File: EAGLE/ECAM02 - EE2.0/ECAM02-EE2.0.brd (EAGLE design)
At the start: 82.6 x 75.9 mm, 61 parts, among them J1 MODULAR TOOL, J2 SPI, J3 MOT, J4 FTDI, J5 S4B-PH-SM4, J6 SOL+PUMP, J7 RINGLIGHT, Q2 16MHz, U1 SP3485, U10 MCP4725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

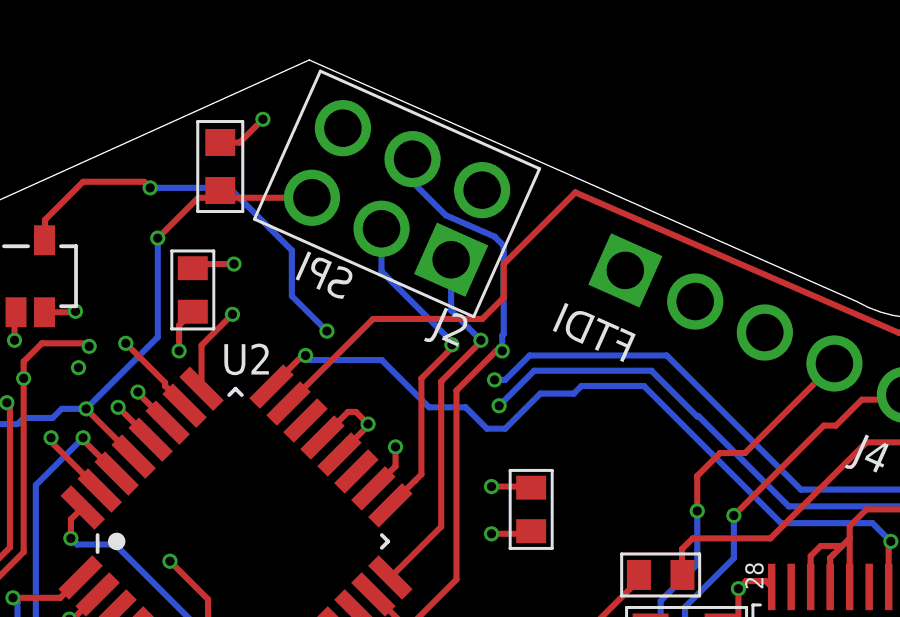
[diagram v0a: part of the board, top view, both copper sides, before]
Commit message: Fixed BOM, began adding DFM changes
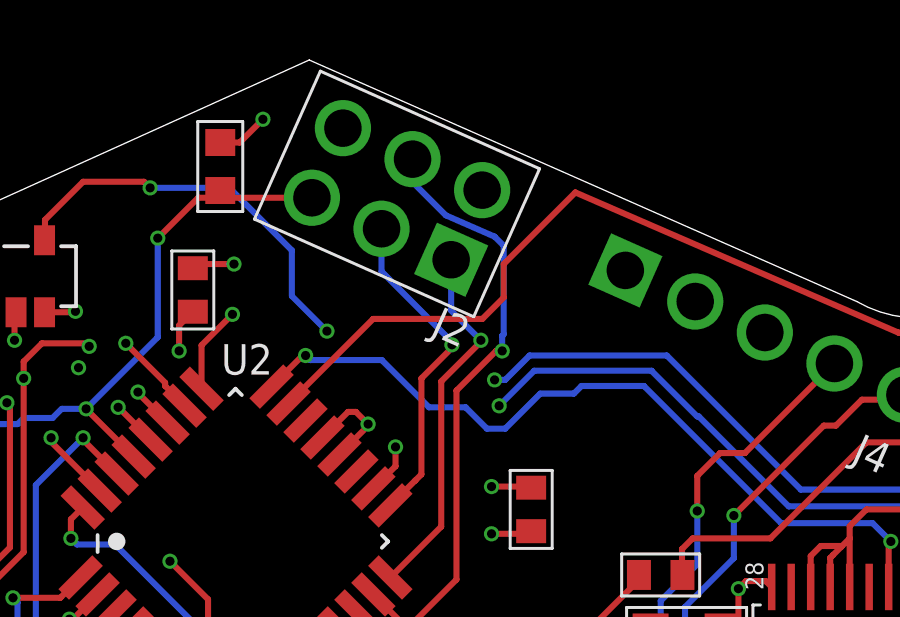
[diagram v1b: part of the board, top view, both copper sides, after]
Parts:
- U11: value NTR4003NT3G -> ZXMN10A07FTA
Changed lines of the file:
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@@
 <?xml version="1.0" encoding="utf-8"?>
 <!DOCTYPE eagle SYSTEM "eagle.dtd">
-<eagle version="7.3.0">
+<eagle version="7.4.0">
 <drawing>
 <settings>
@@
 <layer number="20" name="Dimension" color="15" fill="1" visible="yes" active="yes"/>
 <layer number="21" name="tPlace" color="7" fill="1" visible="yes" active="yes"/>
-<layer number="22" name="bPlace" color="7" fill="1" visible="no" active="yes"/>
+<layer number="22" name="bPlace" color="7" fill="1" visible="yes" active="yes"/>
 <layer number="23" name="tOrigins" color="15" fill="1" visible="yes" active="yes"/>
 <layer number="24" name="bOrigins" color="15" fill="1" visible="no" active="yes"/>
@@
 <circle x="56.96" y="32" radius="3.5" width="0.0001" layer="20"/>
 <circle x="26.6" y="32" radius="8" width="0.0001" layer="20"/>
-<text x="42.50655" y="67.851990625" size="1.016" layer="21" rot="MR24">SPI</text>
-<text x="51.90455" y="65.769190625" size="1.016" layer="21" rot="MR24">FTDI</text>
+<text x="39.230365625" y="69.455096875" size="1.016" layer="22" rot="R336">SPI</text>
+<text x="49.66906875" y="66.98308125" size="1.016" layer="22" rot="R336">FTDI</text>
 <text x="64.928646875" y="32.536546875" size="0.635" layer="21" rot="R86">SOLENOIDS</text>
 <text x="29.238465625" y="18.436003125" size="0.635" layer="21">MOD TOOL</text>
@@
 <attribute name="PARTNO" value="B7B-PH-SM4-TB(LF)(SN)" x="66.19743125" y="33.5224125" size="1.778" layer="27" rot="R264" display="off"/>
 </element>
-<element name="U11" library="TinWhiskers" package="SOT-23-3" value="NTR4003NT3G" x="62.6872" y="31.5468" rot="MR90">
-<attribute name="PARTNO" value="NTR4003NT3G" x="62.6872" y="31.5468" size="1.778" layer="28" rot="MR90" display="off"/>
+<element name="U11" library="TinWhiskers" package="SOT-23-3" value="ZXMN10A07FTA" x="62.6872" y="31.5468" rot="MR90">
+<attribute name="PARTNO" value="ZXMN10A07FTA" x="62.6872" y="31.5468" size="1.778" layer="28" rot="MR90" display="off"/>
 </element>
 <element name="C13" library="TinWhiskers" package="C0603" value="0.1uF" x="48.7172" y="60.9092" smashed="yes" rot="R270">

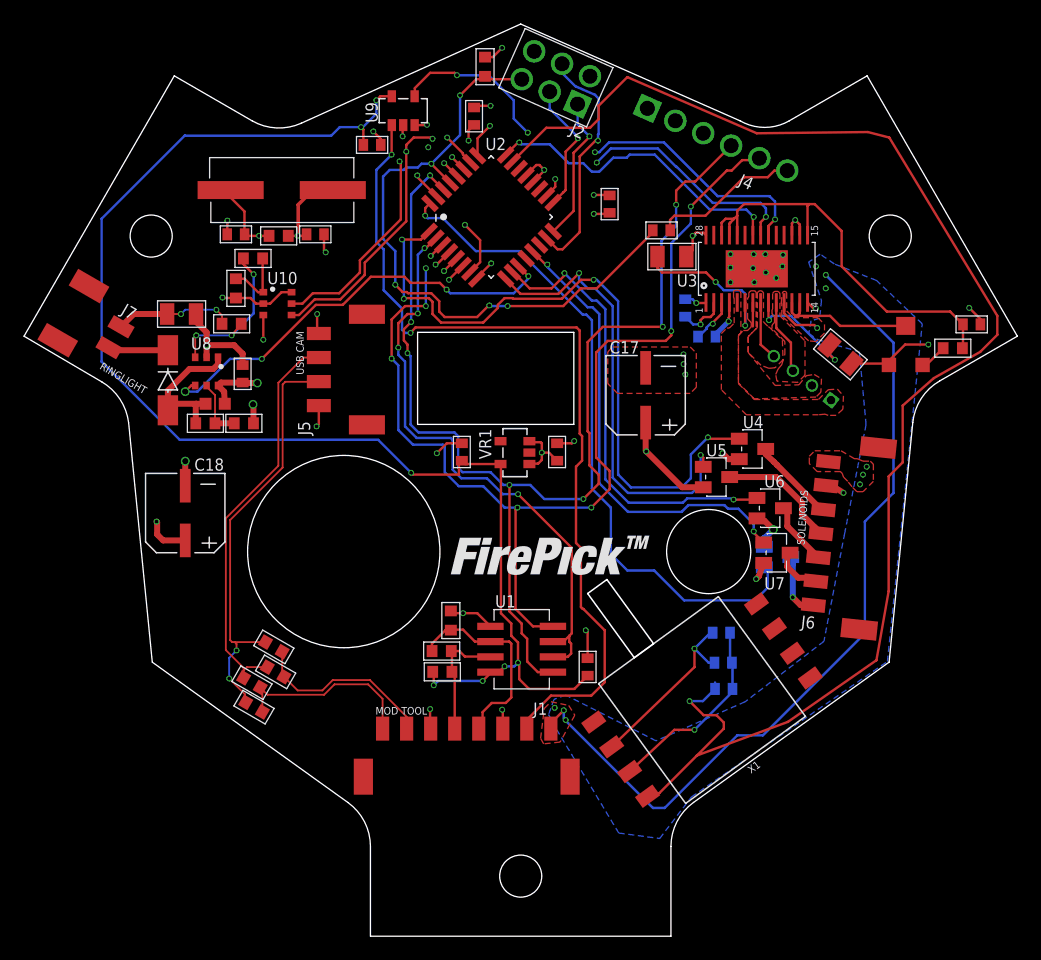
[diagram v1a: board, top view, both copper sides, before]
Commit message: Made REV 2 modifications, including increasing width of power traces, adding vias to power traces, and addition of LEDs to all modular tools. Catch diodes added to ESOL01 board to prevent coils from creating problems "upstream"
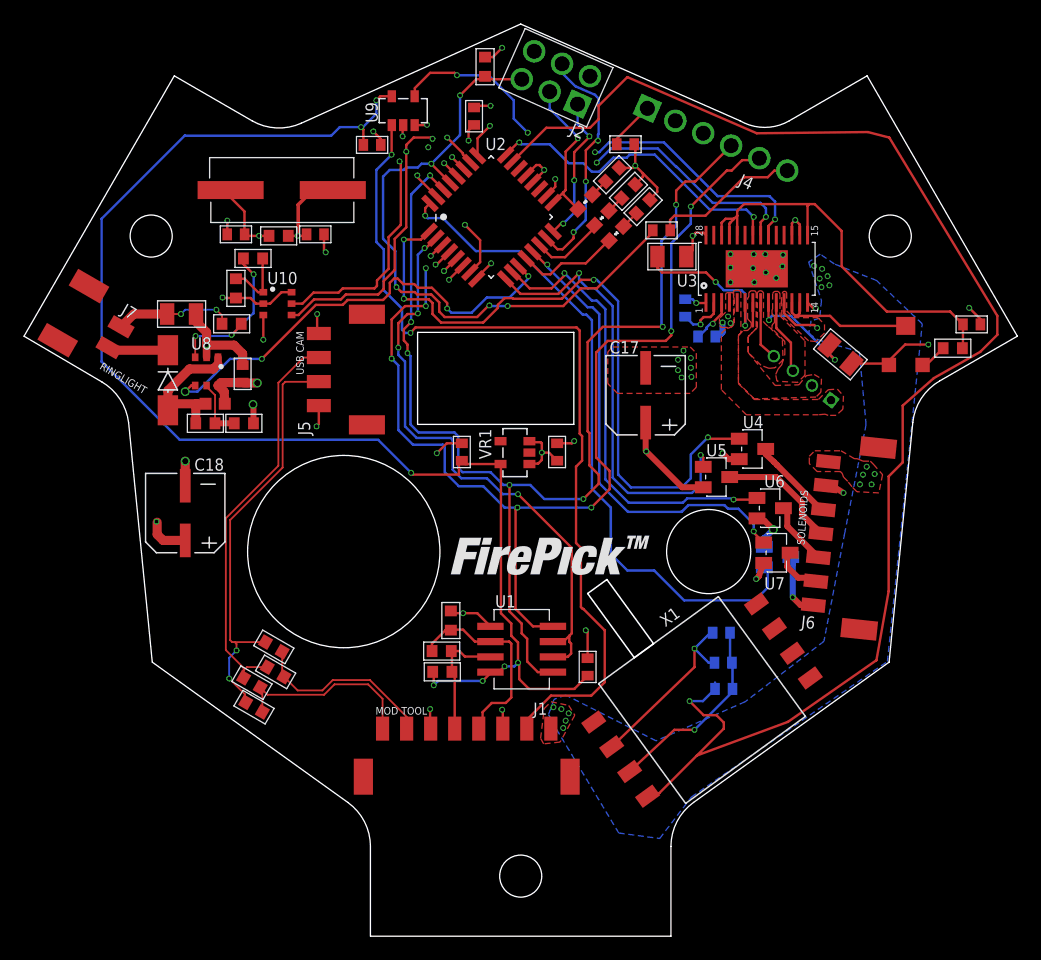
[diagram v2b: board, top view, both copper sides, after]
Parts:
- added LED1, LED2, LED3: RED, TinWhiskers:LED0603
- added R14, R21, R22: 1K, TinWhiskers:R0603
- moved C13 5.15 mm to (50.0, 65.9), turned to 0 degrees
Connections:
- new net N$1: LED1.A, R21.1
- new net N$11: LED3.A, R22.1
- new net N$2: LED2.A, R14.1
- new net N$3: LED1.C, U2.12
- new net N$4: LED2.C, U2.14
- net +5V: now also R14.2, R21.2, R22.2
- net SCK: now also LED3.C
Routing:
- net +24V: track 77.4 -> 6.28 mm, vias 14 -> 27
- net N$3: track 0.00 -> 8.61 mm
- net +5V: track 47.1 -> 54.0 mm
- net N$4: track 0.00 -> 6.22 mm
- net GND: track 93.1 -> 95.8 mm, vias 39 -> 38
- net CTRL: track 36.0 -> 38.0 mm
- net SCK: track 11.0 -> 12.9 mm
- net SDA: track 25.9 -> 27.5 mm
- net N$11: track 0.00 -> 1.55 mm
- net N$1: track 0.00 -> 1.51 mm
- net N$2: track 0.00 -> 1.50 mm
- net SCL: track 23.7 -> 25.2 mm
- net MISO: track 12.3 -> 12.4 mm, vias 1 -> 3
- net MOSI: vias 1 -> 3

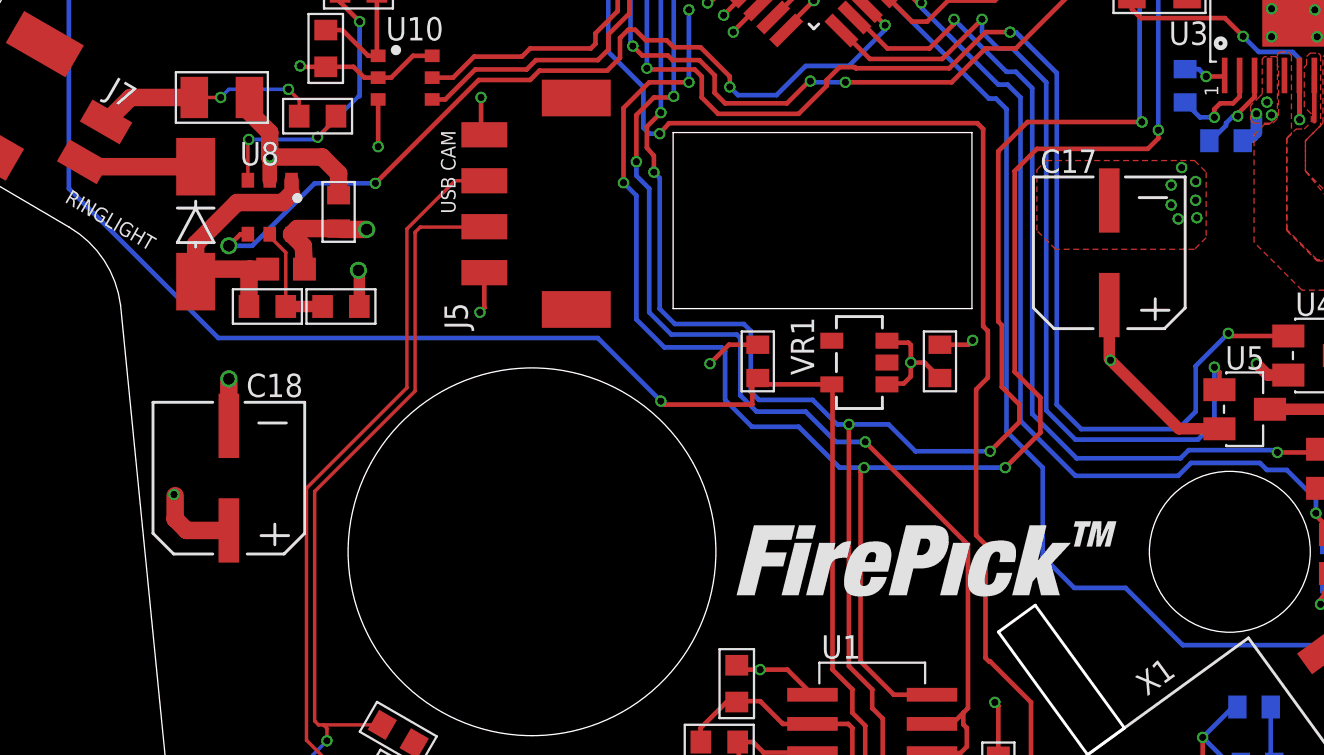
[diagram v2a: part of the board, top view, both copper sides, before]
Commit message: Fixed electrolytic cap reversals on ECAM02
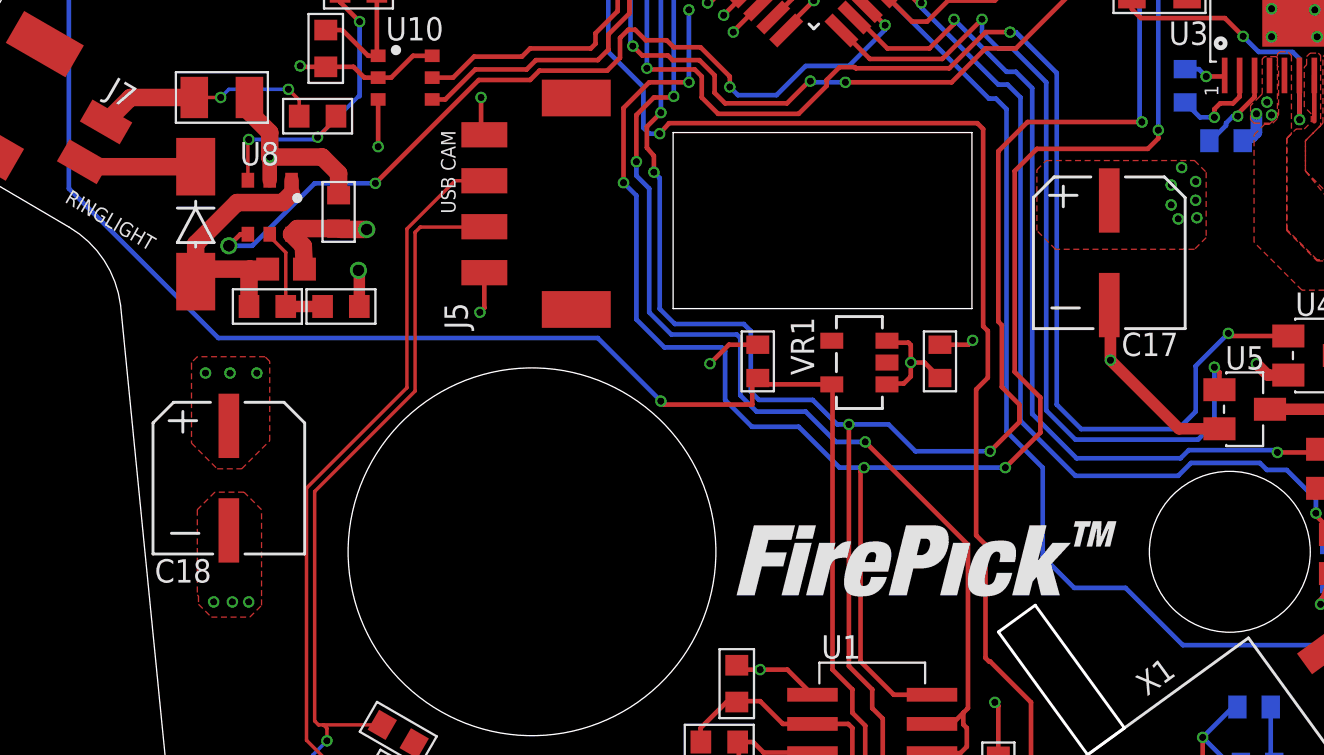
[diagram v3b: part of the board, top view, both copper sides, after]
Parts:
- turned C17 to 0 degrees
- turned C18 to 0 degrees
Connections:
- net +24V: now also C17.POS; no longer C17.NEG
- net +5V: now also C18.POS; no longer C18.NEG
- net GND: now also C17.NEG, C18.NEG; no longer C17.POS, C18.POS
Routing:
- net GND: track 95.8 -> 92.2 mm, vias 38 -> 40
- net +5V: track 54.0 -> 51.9 mm, vias 15 -> 17
- added copper zone on layer 1, net +5V
- added copper zone on layer 1, net GND
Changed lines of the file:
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@@
 <attribute name="PARTNO" value="GMK107BJ104KAHT" x="28.956" y="65.8368" size="1.778" layer="27" rot="R180" display="off"/>
 </element>
-<element name="C17" library="TinWhiskers" package="C-SMD-6.3MM" value="100uF" x="51.7144" y="45.0088" smashed="yes" rot="R180">
-<attribute name="NAME" x="48.7112" y="48.4848" size="1.016" layer="25" font="vector" ratio="12"/>
-<attribute name="VALUE" x="54.5144" y="40.8088" size="0.635" layer="27" font="vector" ratio="12" rot="R180"/>
-<attribute name="PARTNO" value="EMVA500ADA101MHA0G" x="51.7144" y="45.0088" size="1.778" layer="27" rot="R180" display="off"/>
-</element>
-<element name="C18" library="TinWhiskers" package="C-SMD-6.3MM" value="10uF" x="13.4112" y="35.2044" smashed="yes" rot="R180">
-<attribute name="NAME" x="14.1672" y="38.7312" size="1.016" layer="25" font="vector" ratio="12"/>
-<attribute name="VALUE" x="16.2112" y="31.0044" size="0.635" layer="27" font="vector" ratio="12" rot="R180"/>
-<attribute name="PARTNO" value="EMVH350ADA100MF60G" x="13.4112" y="35.2044" size="1.778" layer="27" rot="R180" display="off"/>
+<element name="C17" library="TinWhiskers" package="C-SMD-6.3MM" value="100uF" x="51.7144" y="45.0088" smashed="yes">
+<attribute name="NAME" x="54.7176" y="41.5328" size="1.016" layer="25" font="vector" ratio="12" rot="R180"/>
+<attribute name="VALUE" x="48.9144" y="49.2088" size="0.635" layer="27" font="vector" ratio="12"/>
+<attribute name="PARTNO" value="EMVA500ADA101MHA0G" x="51.7144" y="45.0088" size="1.778" layer="27" display="off"/>
+</element>
+<element name="C18" library="TinWhiskers" package="C-SMD-6.3MM" value="10uF" x="13.4112" y="35.2044" smashed="yes">
+<attribute name="NAME" x="12.6552" y="31.6776" size="1.016" layer="25" font="vector" ratio="12" rot="R180"/>
+<attribute name="VALUE" x="10.6112" y="39.4044" size="0.635" layer="27" font="vector" ratio="12"/>
+<attribute name="PARTNO" value="EMVH350ADA100MF60G" x="13.4112" y="35.2044" size="1.778" layer="27" display="off"/>
 </element>
 <element name="LED1" library="TinWhiskers" package="LED0603" value="RED" x="49.276184375" y="58.463140625" smashed="yes" rot="R225">
@@
 <wire x1="46.8884" y1="23.1278" x2="46.8884" y2="25.2984" width="0.2032" layer="1"/>
 <wire x1="46.8884" y1="25.2984" x2="46.736" y2="25.4508" width="0.2032" layer="1"/>
-<contactref element="C17" pad="POS"/>
-<contactref element="C18" pad="POS"/>
-<wire x1="13.4112" y1="32.9294" x2="11.5714" y2="32.9294" width="0.762" layer="1"/>
-<wire x1="11.5714" y1="32.9294" x2="11.0744" y2="33.4264" width="0.762" layer="1"/>
-<via x="11.0236" y="34.4932" extent="1-16" drill="0.3048"/>
-<wire x1="11.0744" y1="33.4264" x2="11.0744" y2="34.4424" width="0.762" layer="1"/>
-<wire x1="11.0744" y1="34.4424" x2="11.0236" y2="34.4932" width="0.5" layer="1"/>
 <via x="51.7652" y="40.3352" extent="1-16" drill="0.3048"/>
-<wire x1="51.7144" y1="42.7338" x2="51.7144" y2="40.386" width="0.5" layer="1"/>
 <wire x1="51.7144" y1="40.386" x2="51.7652" y2="40.3352" width="0.2032" layer="1"/>
 <wire x1="60.9776" y1="34.7608" x2="61.6068" y2="34.5576" width="0.5" layer="1"/>
@@
 <wire x1="49.313" y1="65.8876" x2="49.313" y2="66.332790625" width="0.2032" layer="1"/>
 <wire x1="49.313" y1="66.332790625" x2="51.856984375" y2="68.876775" width="0.2032" layer="1"/>
+<contactref element="C17" pad="NEG"/>
+<wire x1="51.7144" y1="42.7338" x2="51.7652" y2="42.7338" width="0.4064" layer="1"/>
+<wire x1="51.7652" y1="42.7338" x2="51.7652" y2="40.3352" width="0.508" layer="1"/>
+<contactref element="C18" pad="NEG"/>
+<polygon width="0.0508" layer="1" thermals="no">
+<vertex x="12.0904" y="30.0736"/>
+<vertex x="12.0904" y="29.718"/>
+<vertex x="12.6492" y="29.1592"/>
+<vertex x="14.3256" y="29.1592"/>
+<vertex x="14.8336" y="29.6672"/>
+<vertex x="14.8336" y="30.0736"/>
+<vertex x="14.8336" y="33.8328"/>
+<vertex x="14.0716" y="34.5948"/>
+<vertex x="12.8016" y="34.5948"/>
+<vertex x="12.0396" y="33.8328"/>
+<vertex x="12.0396" y="30.1244"/>
+</polygon>
+<via x="12.7508" y="29.8196" extent="1-16" drill="0.3048"/>
+<via x="13.5636" y="29.8196" extent="1-16" drill="0.3048"/>
+<via x="14.2748" y="29.8196" extent="1-16" drill="0.3048"/>
 </signal>
 <signal name="+24V">
@@
 <vertex x="67.9704" y="40.386"/>
 </polygon>
-<contactref element="C17" pad="NEG"/>
 <polygon width="0.2032" layer="15">
 <vertex x="58.674" y="49.53"/>
@@
 <via x="55.5244" y="46.5328" extent="1-16" drill="0.3048"/>
 <via x="54.7116" y="46.482" extent="1-16" drill="0.3048"/>
+<contactref element="C17" pad="POS"/>
 </signal>
 <signal name="+5V">
@@
 <wire x1="50.763" y1="65.8876" x2="50.8508" y2="65.3426" width="0.2032" layer="1"/>
 <wire x1="50.8508" y1="65.3426" x2="50.8508" y2="64.1096" width="0.2032" layer="1"/>
-<contactref element="C18" pad="NEG"/>
-<wire x1="13.4112" y1="39.5224" x2="13.4112" y2="37.4794" width="0.762" layer="1"/>
-<via x="13.4112" y="39.5224" extent="1-16" drill="0.5"/>
 <wire x1="18.1864" y1="46.0618" x2="18.2742" y2="46.0248" width="0.5" layer="1"/>
 <wire x1="18.2742" y1="46.0248" x2="19.4056" y2="46.0248" width="0.762" layer="1"/>
@@
 <wire x1="49.52455625" y1="63.922003125" x2="50.663203125" y2="63.922003125" width="0.2032" layer="1"/>
 <wire x1="50.663203125" y1="63.922003125" x2="50.8508" y2="64.1096" width="0.2032" layer="1"/>
+<contactref element="C18" pad="POS"/>
+<polygon width="0.0508" layer="1" thermals="no">
+<vertex x="11.7856" y="40.1828"/>
+<vertex x="11.7856" y="36.7284"/>
+<vertex x="12.9032" y="35.6108"/>
+<vertex x="13.97" y="35.6108"/>
+<vertex x="15.1892" y="36.83"/>
+<vertex x="15.1892" y="40.2844"/>
+<vertex x="14.986" y="40.4876"/>
+<vertex x="12.0396" y="40.4876"/>
+<vertex x="11.7856" y="40.2336"/>
+</polygon>
+<via x="12.3952" y="39.7764" extent="1-16" drill="0.3048"/>
+<via x="13.462" y="39.7764" extent="1-16" drill="0.3048"/>
+<via x="14.6304" y="39.7764" extent="1-16" drill="0.3048"/>
 </signal>
 <signal name="A">
